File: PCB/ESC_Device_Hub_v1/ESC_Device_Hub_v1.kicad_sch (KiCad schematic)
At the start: 133 parts, among them J1 Conn_01x04, J10 Conn_01x06, J11 Conn_01x02, J12 Conn_01x02, J13 Conn_01x02, J14 Conn_01x02, J15 Conn_01x02, J16 Conn_01x02, J17 Conn_01x02, J18 Conn_01x02, J19 Conn_01x05, J2 Conn_01x04, J20 Conn_01x01, J21 Conn_01x01, J22 Conn_01x02, J3 Conn_01x04, J4 Conn_01x04, J5 Conn_01x04, J6 Conn_01x04, J7 Conn_01x06, J8 Conn_01x06, J9 Conn_01x06, SW1 SW_Push, SW2 SW_Push, SW3 SW_Coded_SH-7050, U1 ISO1042BQDWVQ1, U10 LM66100DCK, U11 LM66100DCK, U18 USB_Type-C, U2 MCP2562FD-H/MF, U3 IS25LP064D-JLLE, U4 STM32H563RGVx, U6 TLP293, U7 NJM2884U1-33, U8 RFM-0505S, Y1 FC2012SN 32.768K-70NNA0KC0, Y2 XRCGB25M000FFS1AR0

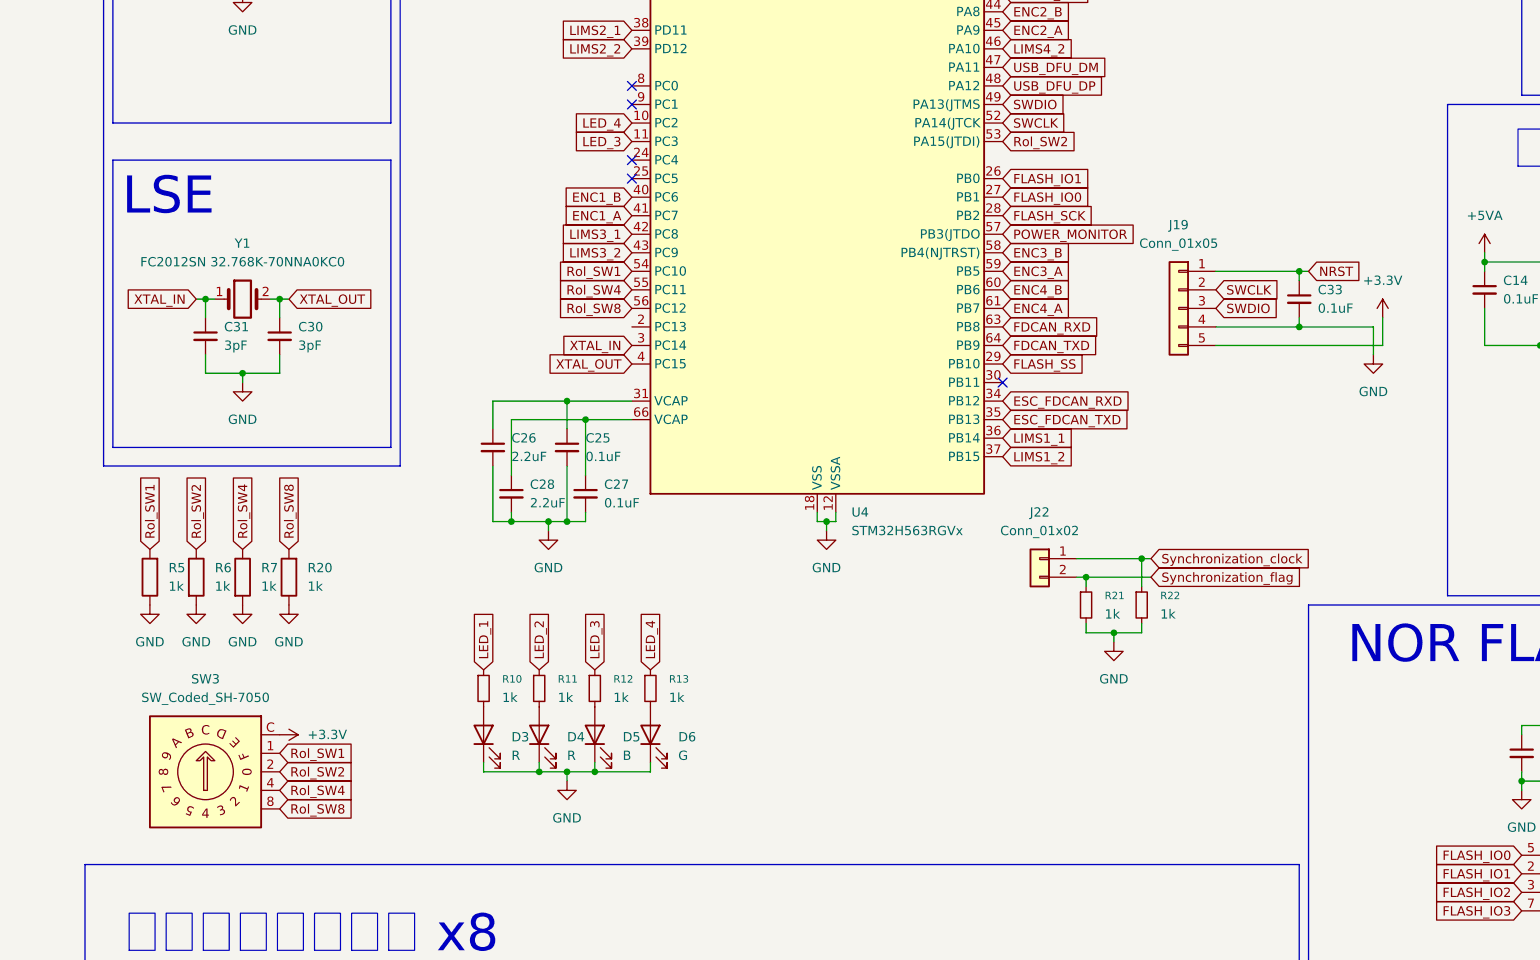
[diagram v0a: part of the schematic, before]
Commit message: PCBの変更 ID変更 NRSTのパスコン一つ減らした
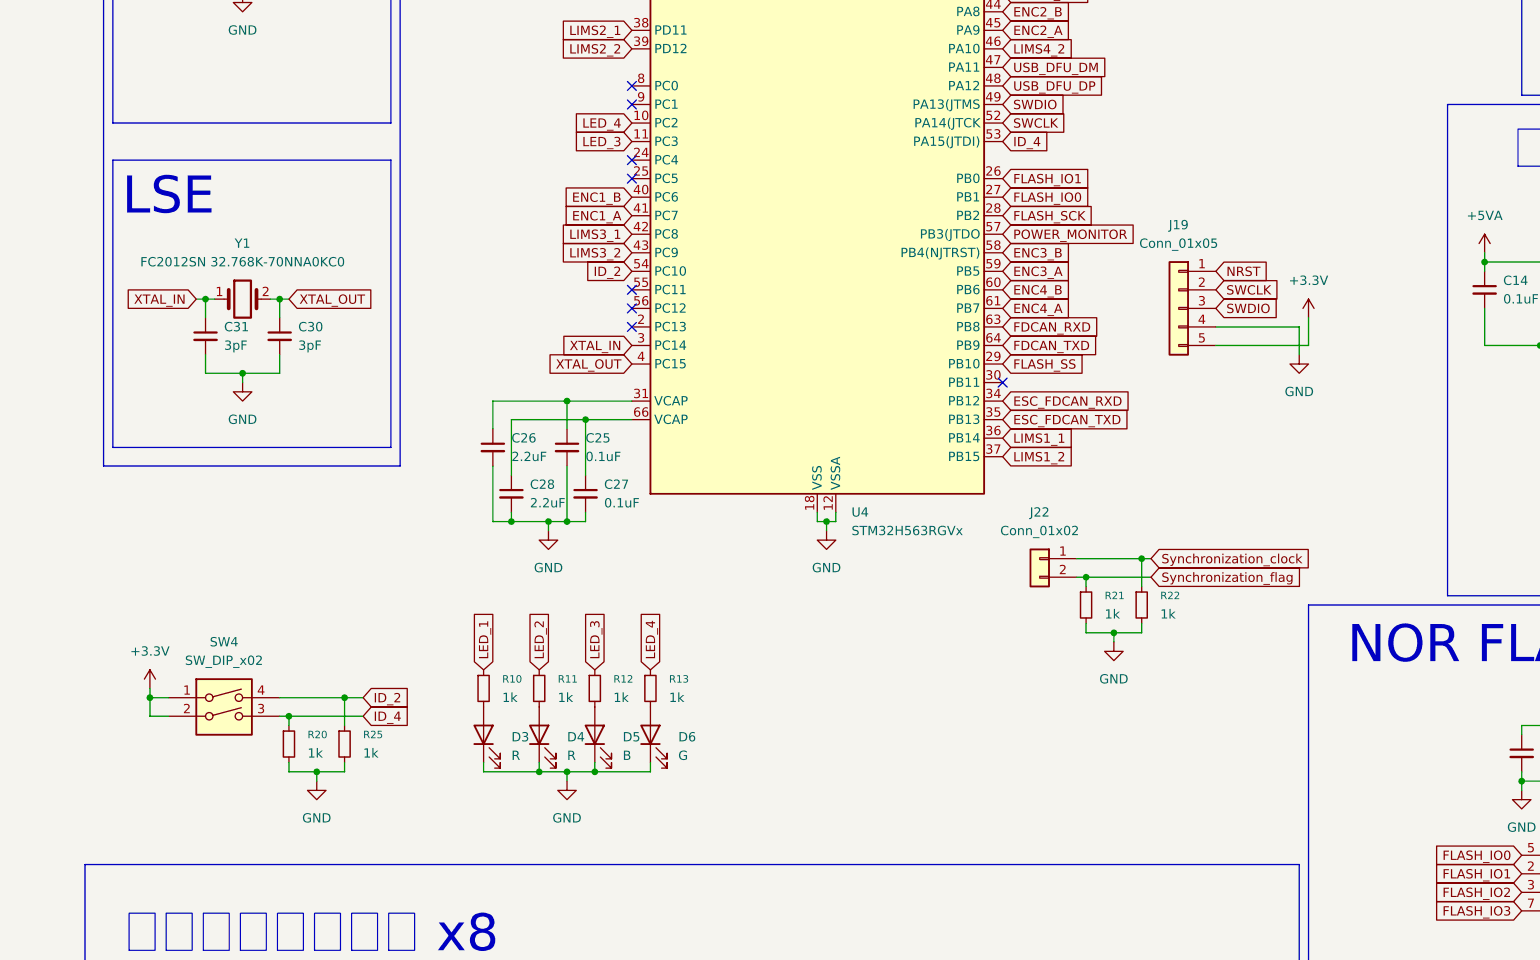
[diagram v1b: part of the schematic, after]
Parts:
- removed C33: 0.1uF, Capacitor_SMD:C_0402_1005Metric_Pad0.74x0.62mm_HandSolder, symbol Device:C_Small
- removed R20, R5, R6, R7: 1k, Resistor_SMD:R_0603_1608Metric_Pad0.98x0.95mm_HandSolder, symbol Device:R
- removed SW3: SW_Coded_SH-7050, My_Library:ERD116RFZ, symbol Switch:SW_Coded_SH-7050
- added R20, R25: 1k, Resistor_SMD:R_0603_1608Metric_Pad0.98x0.95mm_HandSolder, symbol Device:R_Small
- added SW4: SW_DIP_x02, My_Library:KHS22E, symbol Switch:SW_DIP_x02
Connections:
- net +3.3V: now also SW4.1, SW4.2
- net GND: now also R20.2, R25.2
- net Rol_SW1 renamed ID_2
- net ID_2: now also R25.1, SW4.4
- net Rol_SW2 renamed ID_4
- net ID_4: now also R20.1, SW4.3
- net Rol_SW4: no longer names the net of U4.55 (PC11)
- net Rol_SW8: no longer names the net of U4.56 (PC12)
- no-connect marks 10 -> 13

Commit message: 原因不明
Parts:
- removed J19: Conn_01x05, Connector_PinSocket_2.54mm:PinSocket_1x05_P2.54mm_Vertical, symbol Connector_Generic:Conn_01x05
- added J23: Conn_01x04, Connector_PinSocket_2.54mm:PinSocket_1x04_P2.54mm_Vertical, symbol Connector_Generic:Conn_01x04
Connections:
- net +3.3V: now also J23.4 (Pin_4)
- net GND: now also J23.3 (Pin_3)
- net SWCLK: now also J23.1 (Pin_1)
- net SWDIO: now also J23.2 (Pin_2)
